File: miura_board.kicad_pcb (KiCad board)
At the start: 2 copper layers, 60 x 60 mm, 41 parts, among them J1 Screw_Terminal_01x02, J2 Screw_Terminal_01x02, J3 Screw_Terminal_01x02, J4 Conn_01x04_Male, J5 Screw_Terminal_01x02, J6 Screw_Terminal_01x02, J7 Screw_Terminal_01x02, J8 Screw_Terminal_01x02, SW1 SW_Push, SW2 SW_Push, U1 ESP32-WROOM, U2 W25Q32JVSS, U3 DRV8833PW, U4 DRV8833PW, U5 AMS1117, U6 MPU-6050, U7 L7806, U8 DRV8833PW

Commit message: lol
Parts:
- moved U2 19.1 mm to (100.7, 62.0), turned to 0 degrees
- moved U8 9.33 mm to (86.1, 46.1)
- moved C15 7.69 mm to (63.1, 62.6), turned to 90 degrees
- moved U6 4.26 mm to (67.9, 64.6)
- moved J4 3.50 mm to (63.5, 78.0)
- moved C16 2.04 mm to (66.2, 60.2)
- moved R1 1.91 mm to (106.5, 75.0)
- moved C7 1.90 mm to (106.5, 71.4)
- moved U3 0.14 mm to (76.6, 37.7)
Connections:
- J6 pad 2: Net-(J6-Pad2) -> Net-(U3-Pad2)
- U1 pad 10: MOTOR_B12_IN -> MOTOR_A31_IN
- U1 pad 11: MOTOR_B11_IN -> MOTOR_A32_IN
- U1 pad 12: MOTOR_A12_IN -> MOTOR_B31_IN
- U1 pad 13: MOTOR_A11_IN -> MOTOR_B32_IN
- U1 pad 14: unconnected-(U1-Pad14) -> MOTOR_B11_IN
- U1 pad 16: unconnected-(U1-Pad16) -> MOTOR_B12_IN
- U1 pad 23: unconnected-(U1-Pad23) -> MOTOR_A12_IN
- U1 pad 24: unconnected-(U1-Pad24) -> MOTOR_A11_IN
- U1 pad 6: MOTOR_B22_IN -> MOTOR_A21_IN
- U1 pad 7: MOTOR_B21_IN -> MOTOR_A22_IN
- U1 pad 8: MOTOR_A22_IN -> MOTOR_B22_IN
- U1 pad 9: MOTOR_A21_IN -> MOTOR_B21_IN
- U3 pad 2: Net-(J6-Pad1) -> Net-(U3-Pad2)
- U3 pad 4: Net-(J6-Pad2) -> Net-(J6-Pad1)
- U3 pad 5: Net-(J2-Pad2) -> Net-(J2-Pad1)
- U3 pad 7: Net-(J2-Pad1) -> Net-(J2-Pad2)
- U8 pad 10: MOTOR_B22_IN -> MOTOR_B32_IN
- U8 pad 15: MOTOR_A22_IN -> MOTOR_A32_IN
- U8 pad 16: MOTOR_A21_IN -> MOTOR_A31_IN
- U8 pad 9: MOTOR_B21_IN -> MOTOR_B31_IN
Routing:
- net MOTOR_SUPPLY: track 7.20 -> 68.7 mm
- net GND: track 44.6 -> 88.7 mm, vias 14 -> 29
- net MOTOR_B11_IN: track 0.00 -> 31.6 mm
- net MOTOR_B12_IN: track 0.00 -> 29.6 mm
- net MOTOR_A11_IN: track 0.00 -> 27.5 mm
- net MOTOR_A12_IN: track 0.00 -> 26.5 mm
- net MOTOR_B21_IN: track 0.00 -> 20.0 mm, vias 0 -> 2
- net MOTOR_A21_IN: track 0.00 -> 19.7 mm, vias 0 -> 2
- net MOTOR_A22_IN: track 0.00 -> 19.6 mm, vias 0 -> 2
- net Net-(J1-Pad2): track 0.00 -> 19.2 mm, vias 0 -> 1
- net MOTOR_B22_IN: track 0.00 -> 18.8 mm, vias 0 -> 2
- net +3V3: track 26.9 -> 45.7 mm
- net Net-(J1-Pad1): track 0.00 -> 18.7 mm, vias 0 -> 1
- net Net-(J6-Pad1): track 0.00 -> 17.6 mm
- net Net-(J7-Pad1): track 0.00 -> 17.4 mm
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- added copper zone on F.Cu, net +3V3

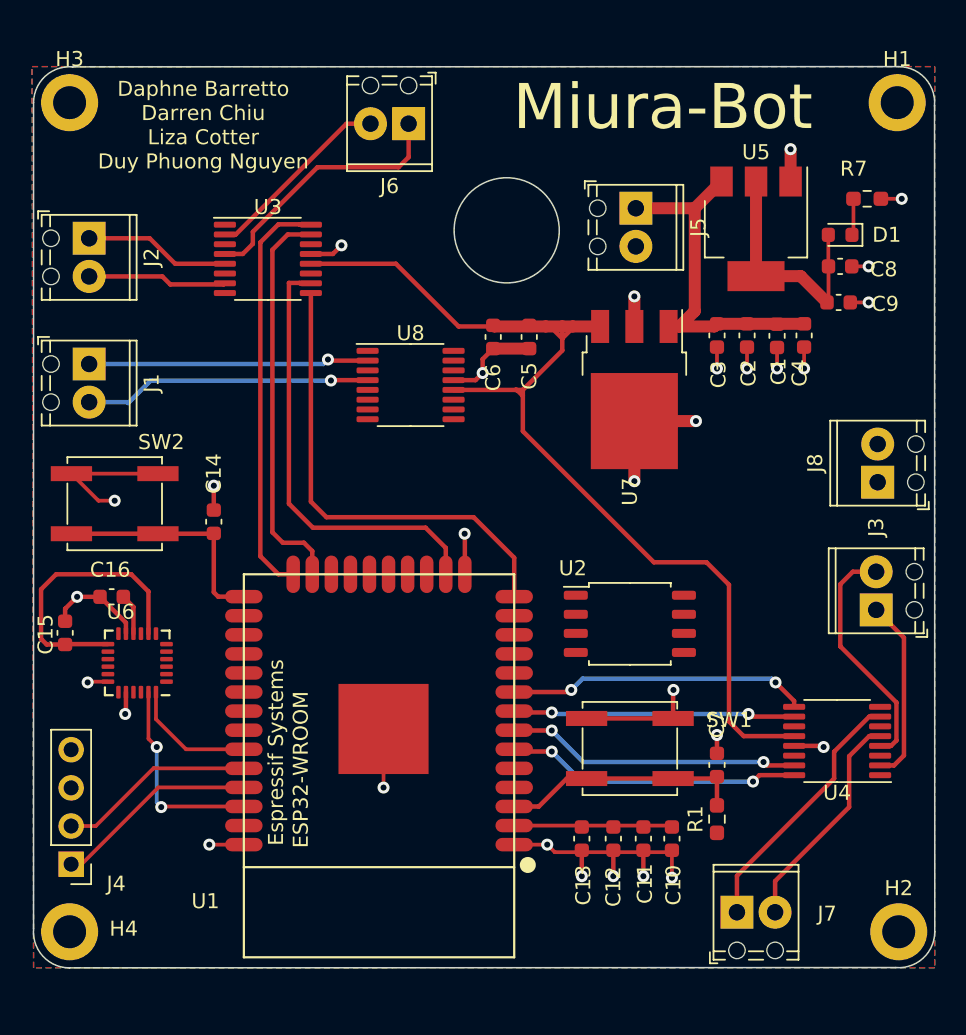
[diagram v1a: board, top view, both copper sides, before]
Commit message: Need to route SPI
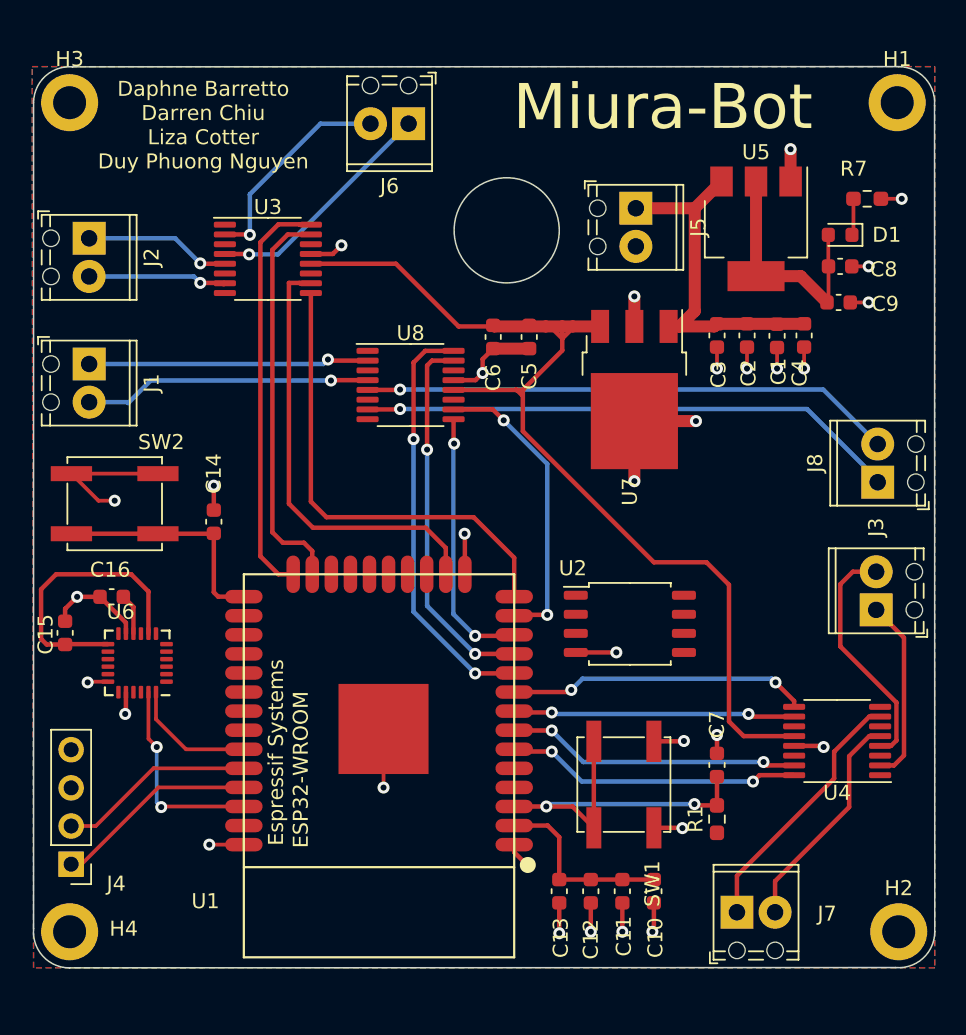
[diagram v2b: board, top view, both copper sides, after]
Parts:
- moved C12 3.81 mm to (98.1, 79.8)
- moved C13 3.81 mm to (96.0, 79.8)
- moved C11 3.77 mm to (100.2, 79.8)
- moved C10 3.70 mm to (102.3, 79.8)
- moved SW1 2.43 mm to (100.3, 72.7), turned to 90 degrees
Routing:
- net Net-(J8-Pad1): track 0.00 -> 36.1 mm, vias 0 -> 1
- net Net-(J8-Pad2): track 0.00 -> 35.5 mm, vias 0 -> 1
- net MOTOR_A31_IN: track 0.00 -> 28.0 mm, vias 0 -> 2
- net MOTOR_A32_IN: track 0.00 -> 25.0 mm, vias 0 -> 2
- net MOTOR_B32_IN: track 0.00 -> 20.0 mm, vias 0 -> 2
- net MOTOR_B31_IN: track 0.00 -> 17.7 mm, vias 0 -> 2
- net GND: track 88.7 -> 79.3 mm, vias 29 -> 31
- net Net-(C7-Pad1): track 16.2 -> 25.5 mm, vias 0 -> 2
- net +3V3: track 45.7 -> 47.5 mm
- net Net-(J6-Pad1): track 17.6 -> 15.8 mm, vias 0 -> 1
- net Net-(U3-Pad2): track 12.7 -> 14.3 mm, vias 0 -> 1
- net Net-(J2-Pad2): track 9.29 -> 9.33 mm, vias 0 -> 1
- net Net-(J2-Pad1): vias 0 -> 1

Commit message: Finished board
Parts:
- moved U2 7.13 mm to (107.6, 60.2)
- moved J6 1.17 mm to (84.8, 28.7)
- moved H2 0.22 mm to (118.7, 82.7)
- moved H4 0.22 mm to (63.3, 82.7)
- moved H1 0.20 mm to (118.7, 27.3)
- moved H3 0.10 mm to (63.3, 27.3)
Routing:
- net MOSI: track 0.00 -> 38.1 mm, vias 0 -> 2
- net SPI_CLK: track 0.00 -> 33.3 mm, vias 0 -> 2
- net MISO: track 0.00 -> 28.4 mm, vias 0 -> 2
- net SPI_CS: track 0.00 -> 24.4 mm, vias 0 -> 2
- net MOTOR_SUPPLY: track 68.7 -> 70.4 mm
- net Net-(U3-Pad2): track 14.3 -> 13.2 mm
- net MOTOR_A32_IN: track 25.0 -> 24.4 mm
- net Net-(C7-Pad1): track 25.5 -> 25.0 mm
- net GND: track 79.3 -> 79.7 mm, vias 31 -> 30
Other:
- outline, holes or cut-outs redrawn

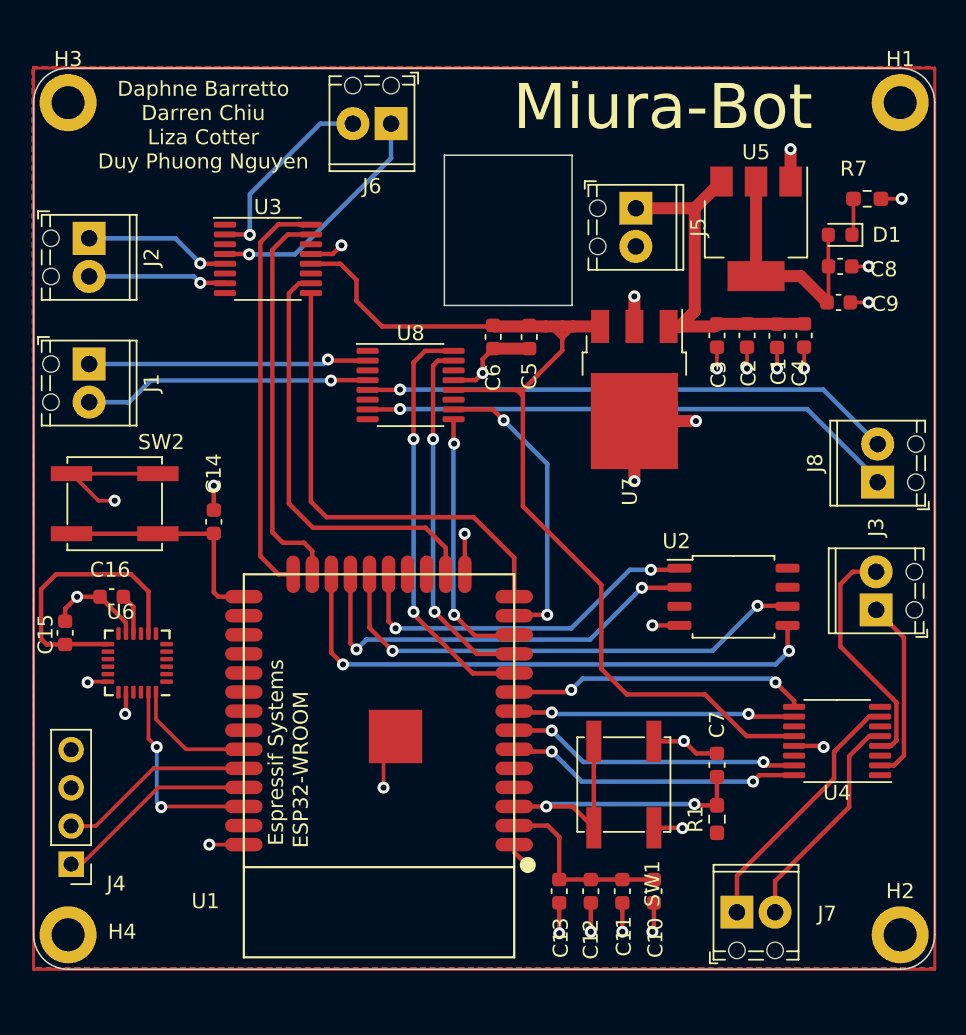
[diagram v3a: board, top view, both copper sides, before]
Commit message: Added more silk
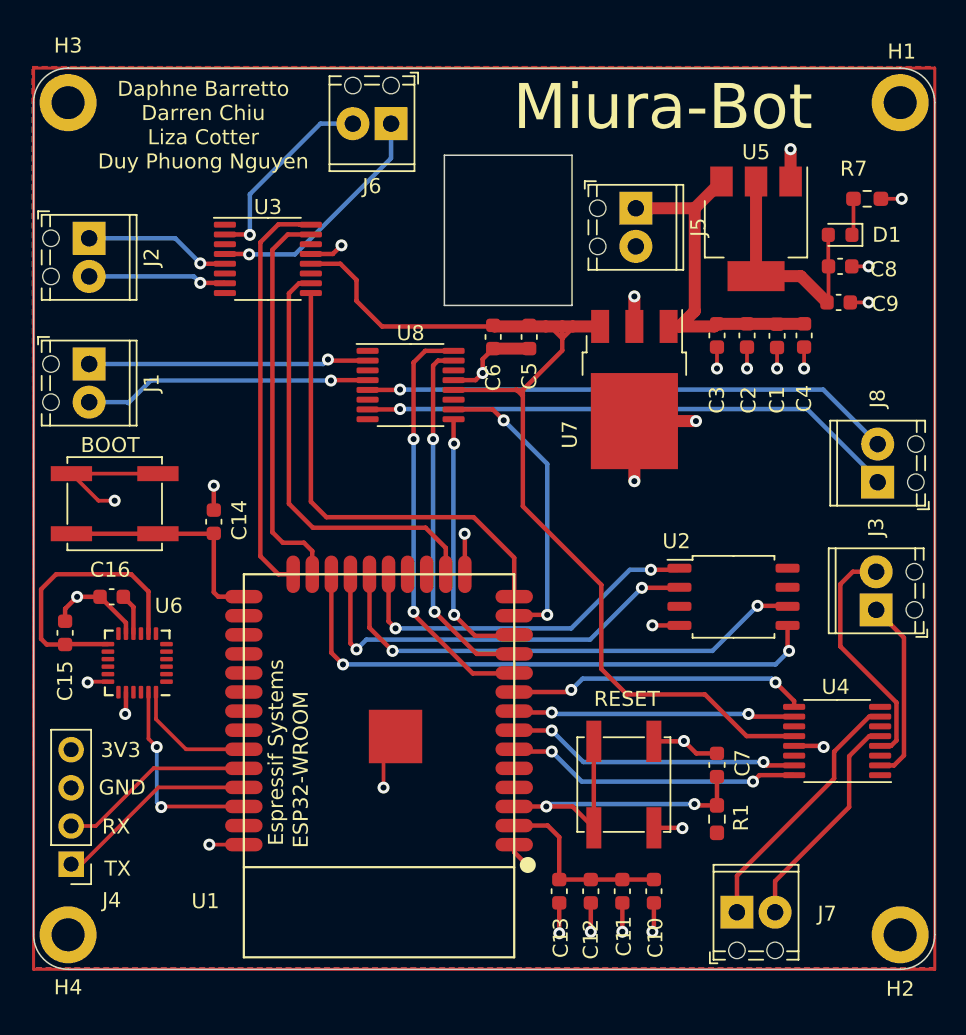
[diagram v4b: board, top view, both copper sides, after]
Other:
- board text added: "3V3"
- board text added: "BOOT"
- board text added: "GND"
- board text added: "RESET"
- board text added: "RX"
- board text added: "TX"
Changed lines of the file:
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@@
     (property "Sheetname" "")
     (attr smd)
-    (fp_text reference "C1" (at 2.375 -0.1 90) (layer "F.SilkS")
+    (fp_text reference "C1" (at 4.275 0 90) (layer "F.SilkS")
       (effects (font (size 1 1) (thickness 0.15)))
     )
@@
     (property "Sheetname" "")
     (attr smd)
-    (fp_text reference "C4" (at 2.5 0.3 90) (layer "F.SilkS")
+    (fp_text reference "C4" (at 4.2 0 90) (layer "F.SilkS")
       (effects (font (size 1 1) (thickness 0.15)))
     )
@@
     (property "Sheetname" "")
     (attr smd)
-    (fp_text reference "C14" (at 3.2 0 90) (layer "F.SilkS")
+    (fp_text reference "C14" (at 0.1 1.7 90) (layer "F.SilkS")
       (effects (font (size 1 1) (thickness 0.15)))
     )
@@
     (property "Sheetname" "")
     (attr smd)
-    (fp_text reference "SW1" (at -6.6 1.9 90) (layer "F.SilkS")
+    (fp_text reference "SW1" (at -5.3 4.2 180) (layer "F.SilkS") hide
       (effects (font (size 1 1) (thickness 0.15)))
     )
@@
     (property "Sheetname" "")
     (attr smd)
-    (fp_text reference "C3" (at 2.6 -0.1 90) (layer "F.SilkS")
+    (fp_text reference "C3" (at 4.3 0 90) (layer "F.SilkS")
       (effects (font (size 1 1) (thickness 0.15)))
     )
@@
     (property "Sheetname" "")
     (attr exclude_from_pos_files)
-    (fp_text reference "H4" (at 3.6 -0.2) (layer "F.SilkS")
+    (fp_text reference "H4" (at 0 3.5) (layer "F.SilkS")
       (effects (font (size 1 1) (thickness 0.15)))
     )
@@
     (property "Sheetname" "")
     (attr smd)
-    (fp_text reference "U4" (at 0 -3.45) (layer "F.SilkS")
+    (fp_text reference "U4" (at 0.1 3.6) (layer "F.SilkS")
       (effects (font (size 1 1) (thickness 0.15)))
     )
@@
     (property "Sheetname" "")
     (attr through_hole)
-    (fp_text reference "J4" (at -3 -1.3) (layer "F.SilkS")
+    (fp_text reference "J4" (at -2.7 -2.4) (layer "F.SilkS")
       (effects (font (size 1 1) (thickness 0.15)))
     )
@@
     (property "Sheetname" "")
     (attr exclude_from_pos_files)
-    (fp_text reference "H1" (at 0 -2.9) (layer "F.SilkS")
+    (fp_text reference "H1" (at 0.1 -3.4) (layer "F.SilkS")
       (effects (font (size 1 1) (thickness 0.15)))
     )
@@
     (property "Sheetname" "")
     (attr smd)
-    (fp_text reference "C15" (at -0.1 -1.3 90) (layer "F.SilkS")
+    (fp_text reference "C15" (at -3.2 0 90) (layer "F.SilkS")
       (effects (font (size 1 1) (thickness 0.15)))
     )
@@
     (property "Sheetname" "")
     (attr exclude_from_pos_files)
-    (fp_text reference "H3" (at 0 -2.9) (layer "F.SilkS")
+    (fp_text reference "H3" (at 0 -3.8) (layer "F.SilkS")
       (effects (font (size 1 1) (thickness 0.15)))
     )
@@
     (property "Sheetname" "")
     (attr smd)
-    (fp_text reference "R1" (at 0 -1.43 90) (layer "F.SilkS")
+    (fp_text reference "R1" (at 0.1 1.6 90) (layer "F.SilkS")
       (effects (font (size 1 1) (thickness 0.15)))
     )
@@
     (property "Sheetname" "")
     (attr smd)
-    (fp_text reference "U6" (at 1.1 3.4) (layer "F.SilkS")
+    (fp_text reference "U6" (at -2.1 3.8) (layer "F.SilkS")
       (effects (font (size 1 1) (thickness 0.15)))
     )
@@
     (property "Sheetname" "")
     (attr through_hole)
-    (fp_text reference "J8" (at 1.27 -4.16 90) (layer "F.SilkS")
+    (fp_text reference "J8" (at 5.57 0 90) (layer "F.SilkS")
       (effects (font (size 1 1) (thickness 0.15)))
     )
@@
     (property "Sheetname" "")
     (attr smd)
-    (fp_text reference "SW2" (at -3.1 4.1) (layer "F.SilkS")
+    (fp_text reference "SW2" (at -3.1 4.1) (layer "F.SilkS") hide
       (effects (font (size 1 1) (thickness 0.15)))
     )
@@
     (property "Sheetname" "")
     (attr smd)
-    (fp_text reference "C2" (at 2.5 -0.1 90) (layer "F.SilkS")
+    (fp_text reference "C2" (at 4.3 -0.1 90) (layer "F.SilkS")
       (effects (font (size 1 1) (thickness 0.15)))
     )
@@
     (property "Sheetname" "")
     (attr exclude_from_pos_files)
-    (fp_text reference "H2" (at 0 -2.9) (layer "F.SilkS")
+    (fp_text reference "H2" (at 0 3.6) (layer "F.SilkS")
       (effects (font (size 1 1) (thickness 0.15)))
     )
@@
     (property "Sheetname" "")
     (attr smd)
-    (fp_text reference "U7" (at 6.8 0.3 90) (layer "F.SilkS")
+    (fp_text reference "U7" (at 3 4.3 90) (layer "F.SilkS")
       (effects (font (size 1 1) (thickness 0.15)))
     )
@@
     (property "Sheetname" "")
     (attr smd)
-    (fp_text reference "C7" (at 2.7 0 90) (layer "F.SilkS")
+    (fp_text reference "C7" (at 0.14058 1.7 90) (layer "F.SilkS")
       (effects (font (size 1 1) (thickness 0.15)))
     )
@@
   (gr_line (start 121 27.3) (end 121 82.7) (layer "Edge.Cuts") (width 0.1))
   (gr_line (start 61 82.7) (end 61 27.3) (layer "Edge.Cuts") (width 0.1))
+  (gr_text "TX" (at 66.6 78.3) (layer "F.SilkS")
+    (effects (font (size 1 1) (thickness 0.15)))
+  )
+  (gr_text "GND" (at 66.9 72.9) (layer "F.SilkS")
+    (effects (font (size 1 1) (thickness 0.15)))
+  )
+  (gr_text "BOOT\n" (at 66.1 50.1) (layer "F.SilkS")
+    (effects (font (size 1 1) (thickness 0.15)))
+  )
+  (gr_text "RX" (at 66.5 75.5) (layer "F.SilkS")
+    (effects (font (size 1 1) (thickness 0.15)))
+  )
+  (gr_text "RESET\n" (at 100.5 67) (layer "F.SilkS")
+    (effects (font (size 1 1) (thickness 0.15)))
+  )
   (gr_text "Miura-Bot\n" (at 102.9 27.6) (layer "F.SilkS")
     (effects (font (size 3 3) (thickness 0.15)))
   )
+  (gr_text "3V3\n" (at 66.8 70.4) (layer "F.SilkS")
+    (effects (font (size 1 1) (thickness 0.15)))
+  )
   (gr_text "Daphne Barretto\nDarren Chiu\nLiza Cotter\nDuy Phuong Nguyen\n" (at 72.3 28.8) (layer "F.SilkS")

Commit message: asf
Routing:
- net GND: track 79.7 -> 86.9 mm, vias 30 -> 32
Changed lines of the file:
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@@
     (property "Sheetname" "")
     (attr smd)
-    (fp_text reference "U7" (at 3 4.3 90) (layer "F.SilkS")
+    (fp_text reference "U7" (at 4.3 4.3 90) (layer "F.SilkS")
       (effects (font (size 1 1) (thickness 0.15)))
     )
@@
   (segment (start 106.5 43.575) (end 106.5 45) (width 0.25) (layer "F.Cu") (net 1))
   (segment (start 64.65 65.85) (end 64.6 65.9) (width 0.25) (layer "F.Cu") (net 1))
+  (segment (start 93 76.7) (end 90.3 76.7) (width 0.3) (layer "F.Cu") (net 1))
   (segment (start 63.1 61.825) (end 63.1 61) (width 0.3) (layer "F.Cu") (net 1))
   (segment (start 94 43.675) (end 91.6 43.675) (width 0.8) (layer "F.Cu") (net 1))
   (segment (start 111.4 32.55) (end 111.4 30.4) (width 0.8) (layer "F.Cu") (net 1))
   (segment (start 113.525 70.125) (end 113.6 70.2) (width 0.3) (layer "F.Cu") (net 1))
+  (segment (start 111.4 32.55) (end 113.25 32.55) (width 0.8) (layer "F.Cu") (net 1))
   (segment (start 111.6375 70.125) (end 113.525 70.125) (width 0.3) (layer "F.Cu") (net 1))
   (segment (start 67.15 62.65) (end 67.15 61.925) (width 0.3) (layer "F.Cu") (net 1))
@@
   (segment (start 80.925 37.375) (end 81.5 36.8) (width 0.3) (layer "F.Cu") (net 1))
   (segment (start 102.3 80.575) (end 102.3 82.4) (width 0.3) (layer "F.Cu") (net 1))
+  (segment (start 101 48.5) (end 96.6 48.5) (width 0.8) (layer "F.Cu") (net 1))
   (segment (start 96 80.575) (end 96 82.6) (width 0.3) (layer "F.Cu") (net 1))
   (segment (start 104.18 75.58) (end 104.2 75.6) (width 0.3) (layer "F.Cu") (net 1))
@@
   (segment (start 101 48.5) (end 101 52.5) (width 0.8) (layer "F.Cu") (net 1))
   (segment (start 117.4125 33.7) (end 118.8 33.7) (width 0.25) (layer "F.Cu") (net 1))
-  (segment (start 93 77.2) (end 93.9 78.1) (width 0.3) (layer "F.Cu") (net 1))
+  (segment (start 113.25 32.55) (end 113.3 32.6) (width 0.8) (layer "F.Cu") (net 1))
   (segment (start 65.95 65.85) (end 64.65 65.85) (width 0.25) (layer "F.Cu") (net 1))
-  (segment (start 93 76.7) (end 93 77.2) (width 0.3) (layer "F.Cu") (net 1))
   (segment (start 63.52 52) (end 65.32 53.8) (width 0.25) (layer "F.Cu") (net 1))
   (segment (start 67.15 67.95) (end 67.1 68) (width 0.3) (layer "F.Cu") (net 1))
   (segment (start 102.3 69.82) (end 104.28 69.82) (width 0.3) (layer "F.Cu") (net 1))
   (segment (start 104.28 69.82) (end 104.3 69.8) (width 0.3) (layer "F.Cu") (net 1))
+  (via (at 90.3 76.7) (size 0.8) (drill 0.4) (layers "F.Cu" "B.Cu") (net 1))
+  (via (at 96.6 48.5) (size 0.8) (drill 0.4) (layers "F.Cu" "B.Cu") (net 1))
   (via (at 112.3 45) (size 0.8) (drill 0.4) (layers "F.Cu" "B.Cu") (net 1))
   (via (at 106.5 45) (size 0.8) (drill 0.4) (layers "F.Cu" "B.Cu") (net 1))
@@
   (via (at 116.6 38.2) (size 0.8) (drill 0.4) (layers "F.Cu" "B.Cu") (net 1))
   (via (at 104.2 75.6) (size 0.8) (drill 0.4) (layers "F.Cu" "B.Cu") (net 1))
-  (via (at 93.9 78.1) (size 0.8) (drill 0.4) (layers "F.Cu" "B.Cu") (net 1))
   (via (at 98.1 82.5) (size 0.8) (drill 0.4) (layers "F.Cu" "B.Cu") (net 1))
   (via (at 116.6 40.6) (size 0.8) (drill 0.4) (layers "F.Cu" "B.Cu") (net 1))
@@
   (via (at 84.3 72.9) (size 0.8) (drill 0.4) (layers "F.Cu" "B.Cu") (net 1))
   (via (at 110.5 45) (size 0.8) (drill 0.4) (layers "F.Cu" "B.Cu") (net 1))
+  (via (at 113.3 32.6) (size 0.8) (drill 0.4) (layers "F.Cu" "B.Cu") (net 1))
   (via (at 113.6 70.2) (size 0.8) (drill 0.4) (layers "F.Cu" "B.Cu") (net 1))
   (via (at 102.2 82.5) (size 0.8) (drill 0.4) (layers "F.Cu" "B.Cu") (net 1))
